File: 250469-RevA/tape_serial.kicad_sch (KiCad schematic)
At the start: 21 parts, among them J3 Conn_02x6_Edge, J4 DIN-6, Q1 2SD313, Q2 2SC1815

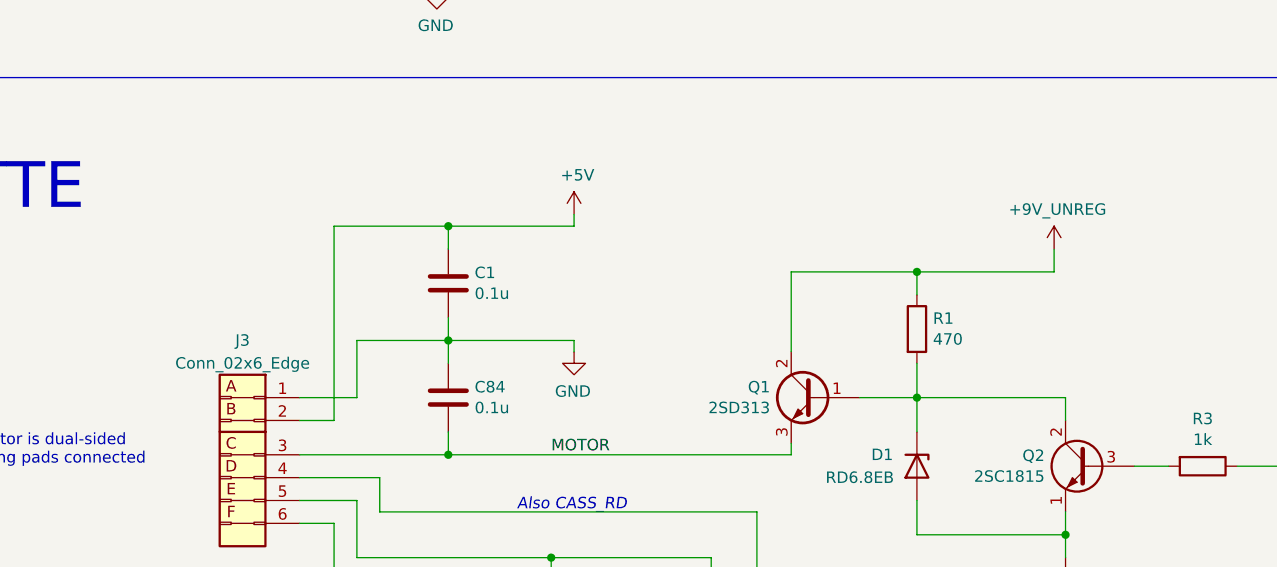
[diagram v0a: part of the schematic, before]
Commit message: Fixes after renaming the project library
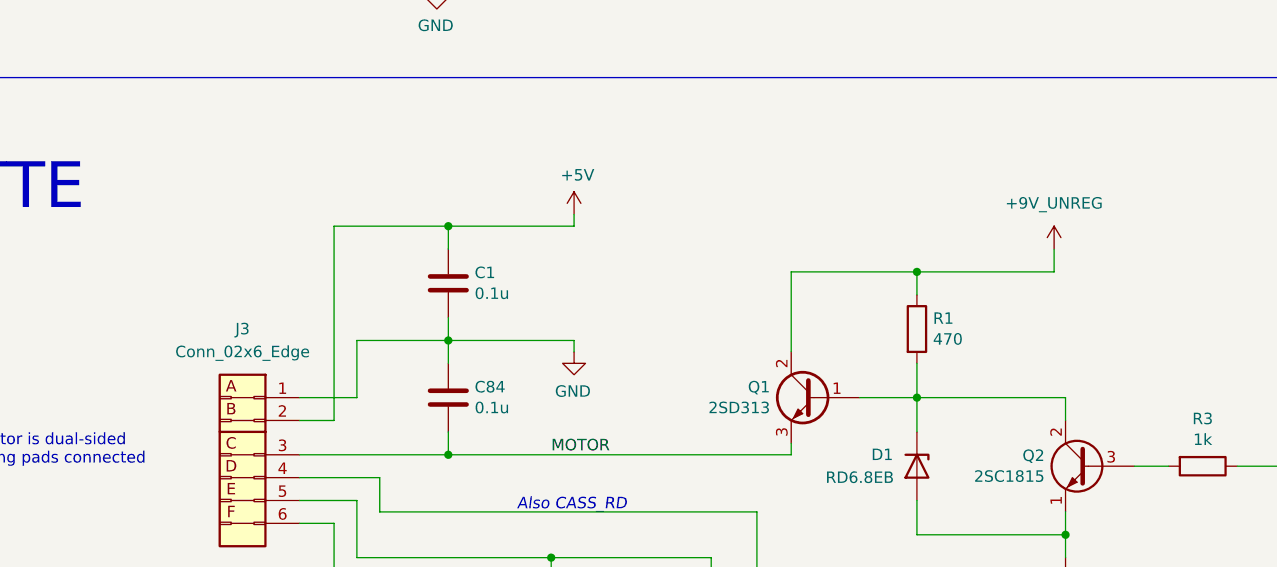
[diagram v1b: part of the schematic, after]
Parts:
- removed J3: Conn_02x6_Edge, 250469-01:Connector_Edge_2x6_P3.96mm, symbol 250469-01:Conn_02x6_Edge
- added J3: Conn_02x6_Edge, C64-C-250469:Connector_Edge_2x6_P3.96mm, symbol C64-C-250469:Conn_02x6_Edge
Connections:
- net +5V: now also J3.2 (Pin_2)
- net C_SENSE: now also J3.6 (Pin_6)
- net C_WRITE: now also J3.5 (Pin_5)
- net GND: now also J3.1 (Pin_1)
- net MOTOR: now also J3.3 (Pin_3)
- net ~{SRQ}: now also J3.4 (Pin_4)
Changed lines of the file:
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@@
-    )
-  )
-  (symbol (lib_id "250469-01:Conn_02x6_Edge") (at 82.55 139.7 0) (mirror y) (unit 1)
-    (in_bom yes) (on_board yes) (dnp no)
-    (property "Reference" "J3" (at 82.55 125.73 0)
-      (effects (font (size 1.27 1.27)))
-    )
-    (property "Value" "Conn_02x6_Edge" (at 82.55 128.27 0)
-      (effects (font (size 1.27 1.27)))
-    )
-    (property "Footprint" "250469-01:Connector_Edge_2x6_P3.96mm" (at 83.82 144.78 0)
-      (effects (font (size 1.27 1.27)) hide)
-    )
-    (property "Datasheet" "" (at 83.82 144.78 0)
-      (effects (font (size 1.27 1.27)) hide)
-    )
-    (pin "1")
-    (pin "2")
-    (pin "3")
-    (pin "4")
-    (pin "5")
-    (pin "6")
-    (instances
-      (project "C64C-250469-01-A"
-        (path "/ceb6c8ef-b249-4909-95e5-e7359667aee8/00000000-0000-0000-0000-00005e2fb209"
-          (reference "J3") (unit 1)
-        )
-      )
-    )
-  )
-  (symbol (lib_id "250469-01:+9V_UNREG") (at 172.72 115.57 0) (unit 1)
-    (in_bom yes) (on_board yes) (dnp no)
-    (property "Reference" "#PWR01" (at 172.72 119.38 0)
-      (effects (font (size 1.27 1.27)) hide)
-    )
-    (property "Value" "+9V_UNREG" (at 173.101 111.1758 0)
-      (effects (font (size 1.27 1.27)))
-    )
-    (property "Footprint" "" (at 172.72 115.57 0)
-      (effects (font (size 1.27 1.27)) hide)
-    )
-    (property "Datasheet" "" (at 172.72 115.57 0)
-      (effects (font (size 1.27 1.27)) hide)
-    )
-    (pin "1")
-    (instances
-      (project "C64C-250469-01-A"
-        (path "/ceb6c8ef-b249-4909-95e5-e7359667aee8/00000000-0000-0000-0000-00005e2fb209"
-          (reference "#PWR01") (unit 1)
-        )
-      )
     )
   )
@@
         )
       )
+    )
+  )
+  (symbol (lib_id "C64-C-250469:Conn_02x6_Edge") (at 82.55 139.7 0) (mirror y) (unit 1)
+    (in_bom yes) (on_board yes) (dnp no) (fields_autoplaced)
+    (property "Reference" "J3" (at 82.55 124.46 0)
+      (effects (font (size 1.27 1.27)))
+    )
+    (property "Value" "Conn_02x6_Edge" (at 82.55 127 0)
+      (effects (font (size 1.27 1.27)))
+    )
+    (property "Footprint" "C64-C-250469:Connector_Edge_2x6_P3.96mm" (at 83.82 144.78 0)
+      (effects (font (size 1.27 1.27)) hide)
+    )
+    (property "Datasheet" "" (at 83.82 144.78 0)
+      (effects (font (size 1.27 1.27)) hide)
+    )
+    (pin "1")
+    (pin "2")
+    (pin "3")
+    (pin "4")
+    (pin "5")
+    (pin "6")
+    (instances
+      (project "C64C-250469-01-A"
+        (path "/ceb6c8ef-b249-4909-95e5-e7359667aee8/00000000-0000-0000-0000-00005e2fb209"
+          (reference "J3") (unit 1)
+        )
+      )
+    )
+  )
+  (symbol (lib_id "C64-C-250469:+9V_UNREG") (at 172.72 115.57 0) (unit 1)
+    (in_bom yes) (on_board yes) (dnp no) (fields_autoplaced)
+    (property "Reference" "#PWR01" (at 172.72 119.38 0)
+      (effects (font (size 1.27 1.27)) hide)
+    )
+    (property "Value" "+9V_UNREG" (at 172.72 110.49 0)
+      (effects (font (size 1.27 1.27)))
+    )
+    (property "Footprint" "" (at 172.72 115.57 0)
+      (effects (font (size 1.27 1.27)) hide)
+    )
+    (property "Datasheet" "" (at 172.72 115.57 0)
+      (effects (font (size 1.27 1.27)) hide)
+    )
+    (pin "1")
+    (instances
+      (project "C64C-250469-01-A"
+        (path "/ceb6c8ef-b249-4909-95e5-e7359667aee8/00000000-0000-0000-0000-00005e2fb209"
+          (reference "#PWR01") (unit 1)
+        )
+      )
